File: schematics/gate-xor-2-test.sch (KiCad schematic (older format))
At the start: 3 parts

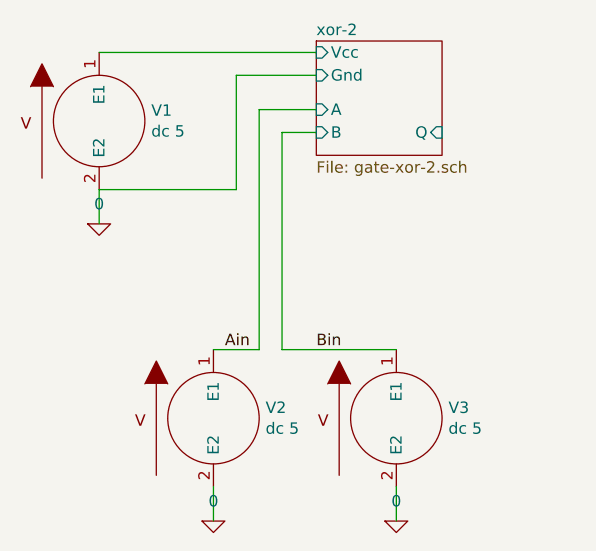
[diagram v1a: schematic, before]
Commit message: Adds a model injector and an op test injector
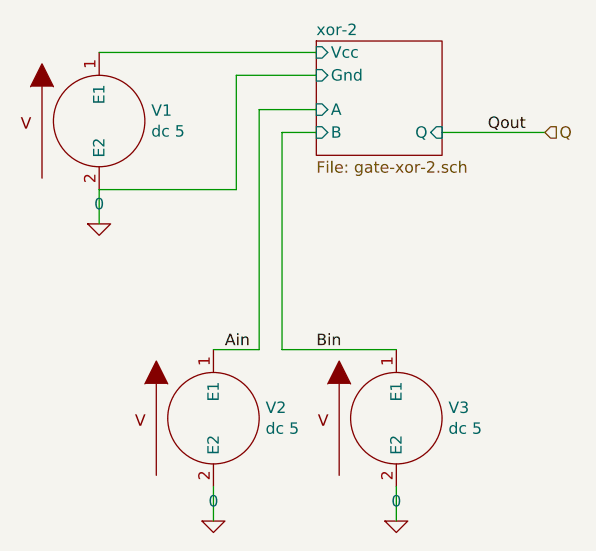
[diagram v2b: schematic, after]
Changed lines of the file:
@@
 Text Label 3100 4150 0    50   ~ 0
 Bin
+Text HLabel 4100 3200 2    50   Input ~ 0
+Q
+Wire Wire Line
+	4100 3200 3650 3200
+Text Label 3850 3200 0    50   ~ 0
+Qout
 $EndSCHEMATC
